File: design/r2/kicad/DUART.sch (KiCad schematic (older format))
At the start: 17 parts, among them IC4 XR68C681CJTR-F, J1 UART_A, J2 UART_B, J4 Conn_01x06, J7 Conn_01x01_Male, Q1 Crystal

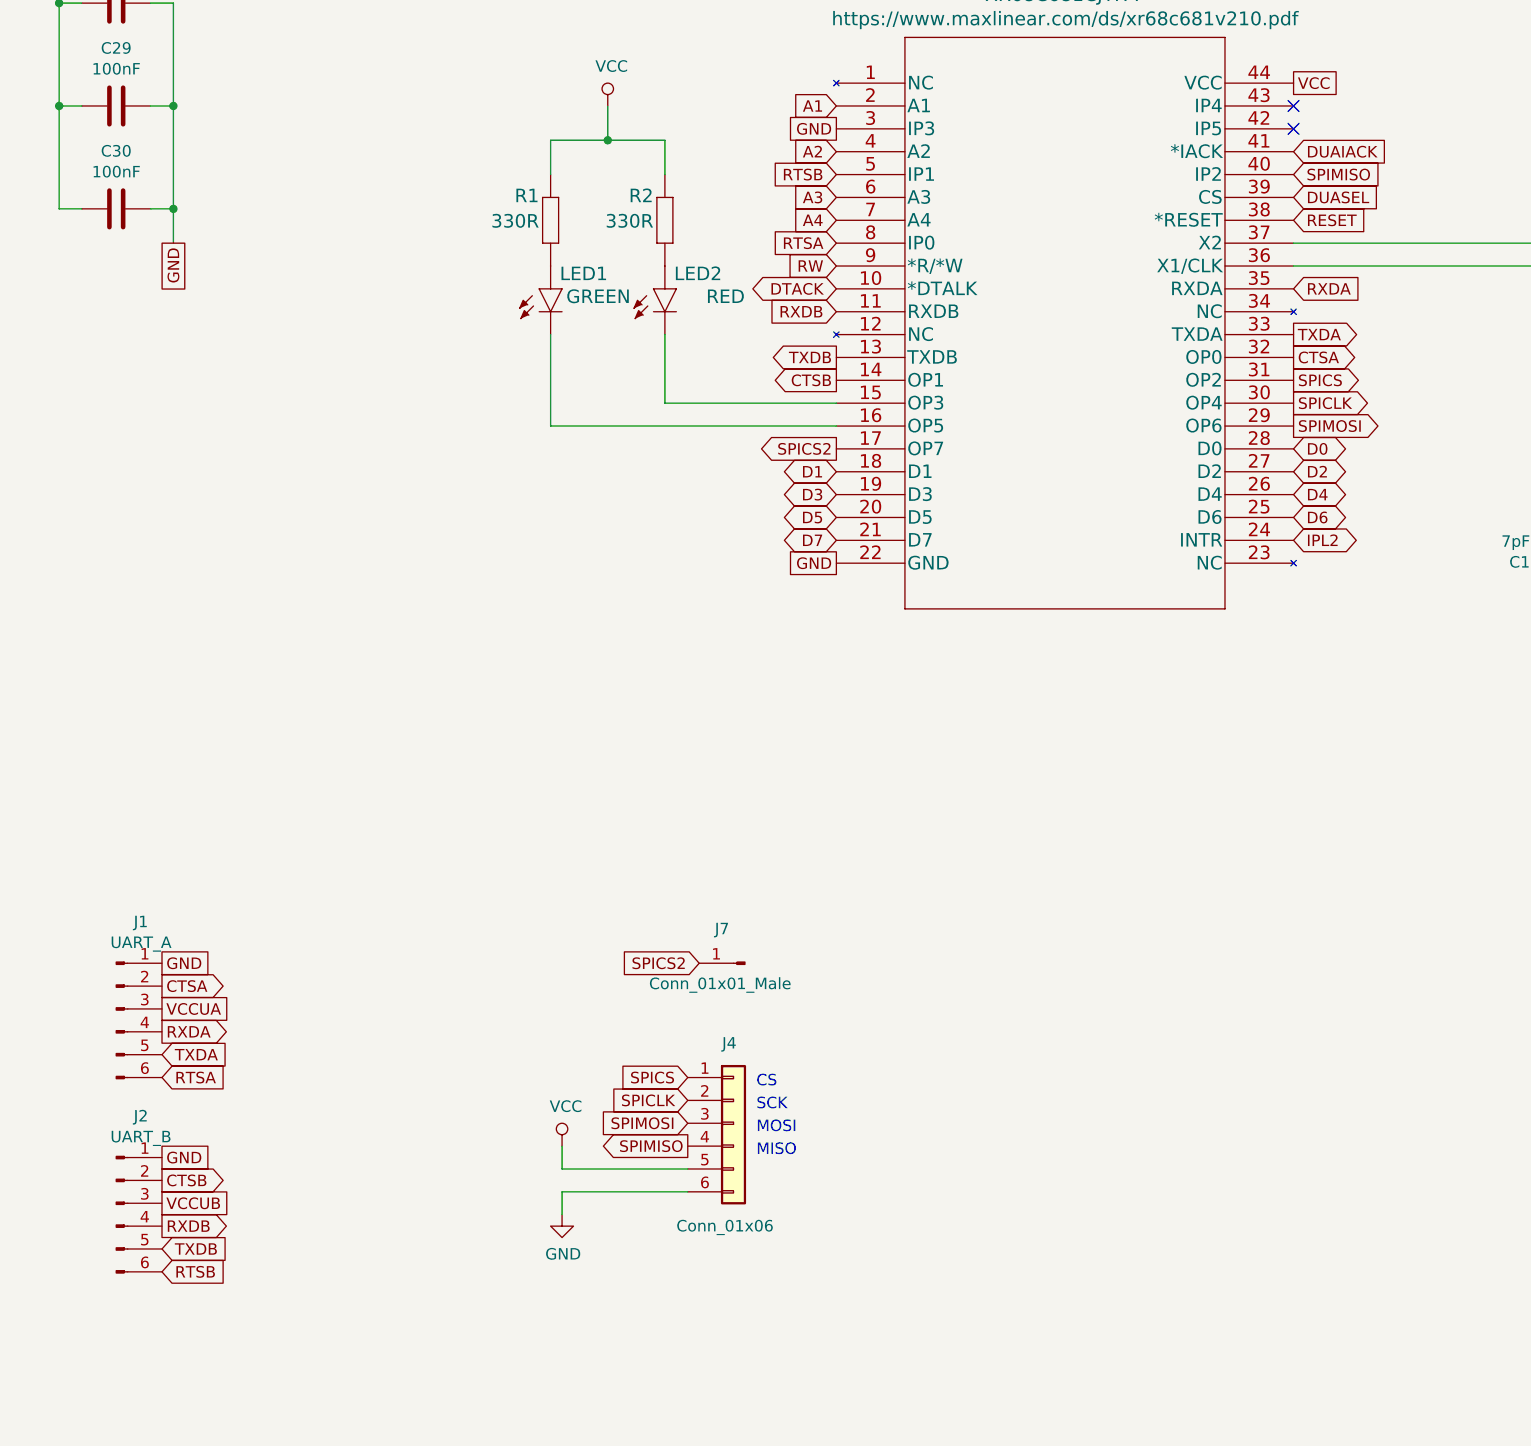
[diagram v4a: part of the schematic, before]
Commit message: Fix CTS/RTS labelling
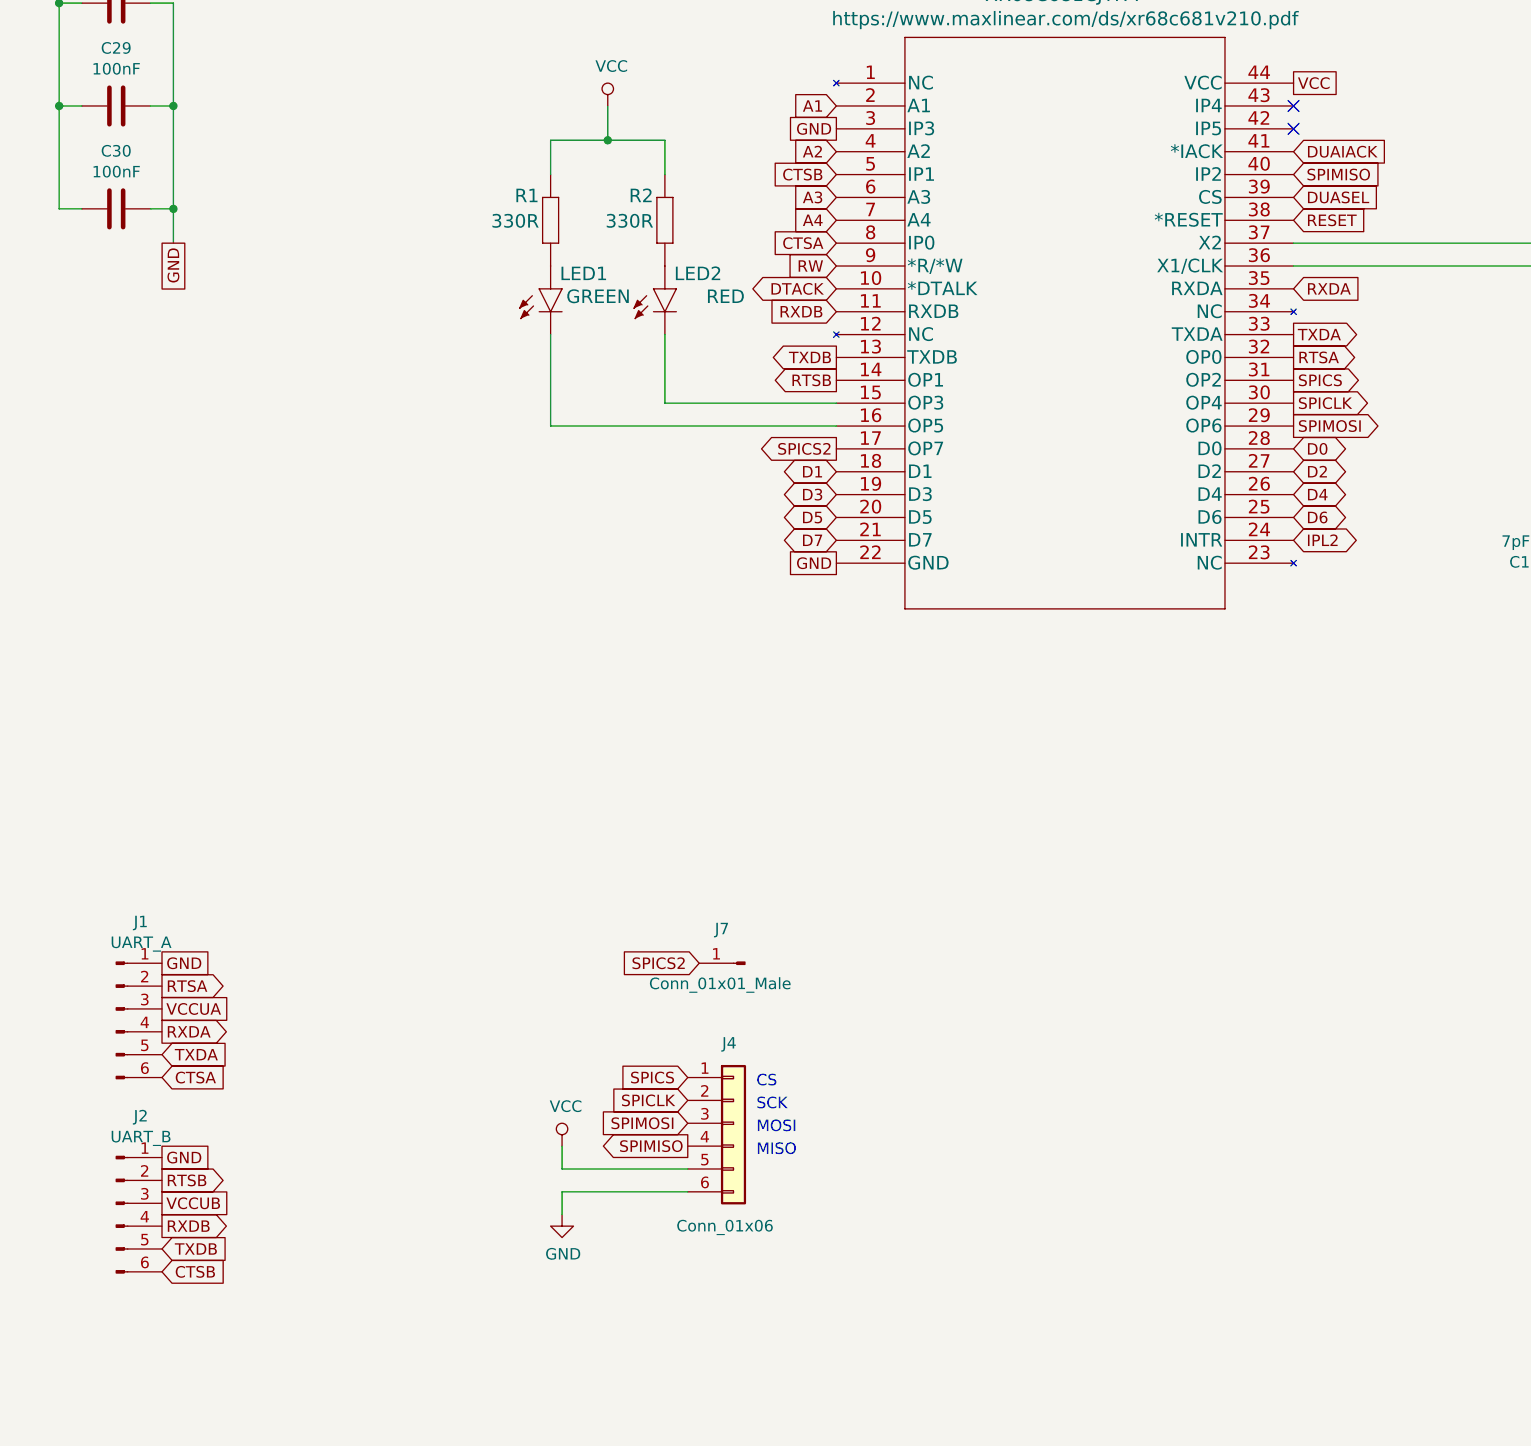
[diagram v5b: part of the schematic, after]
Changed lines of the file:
@@
 GND
 Text GLabel 1450 5750 2    50   Output ~ 0
-CTSA
+RTSA
 Text GLabel 1450 6050 2    50   Input ~ 0
 TXDA
@@
 GND
 Text GLabel 1450 6600 2    50   Output ~ 0
-CTSB
+RTSB
 Text GLabel 1450 6900 2    50   Input ~ 0
 TXDB
@@
 SPIMOSI
 Text GLabel 4400 2500 0    50   Input ~ 0
-RTSA
+CTSA
 Text GLabel 4400 2200 0    50   Input ~ 0
-RTSB
+CTSB
 Text GLabel 6400 2200 2    50   Input ~ 0
 SPIMISO
@@
 GND
 Text GLabel 6400 3000 2    50   Output ~ 0
-CTSA
+RTSA
 Text GLabel 4400 3100 0    50   Output ~ 0
-CTSB
+RTSB
 $Comp
 L Device:C C30
@@
 	9500 5650 9700 5650
 Text GLabel 1450 6150 2    50   Input ~ 0
-RTSA
+CTSA
 Text GLabel 1450 7000 2    50   Input ~ 0
-RTSB
+CTSB
 $Comp
 L rosco_m68k-eagle-import:R-EU_0207_10 R?

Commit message: Bite the bullet and do IPL properly...
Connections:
- net labels added: DUAIRQ
- net labels removed: IPL2
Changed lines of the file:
@@
 Sheet 3 7
 Title "ROSCO_M68K GENERAL PURPOSE MC68010 COMPUTER"
-Date "2021-10-08"
-Rev "2.0"
+Date "2021-10-22"
+Rev "2.1"
 Comp "The Really Old-School Company Limited"
 Comment1 "OSHWA UK000006 (https://certification.oshwa.org/uk000006.html)"
@@
 	8200 2500 6400 2500
 Text GLabel 6400 3800 2    50   3State ~ 0
-IPL2
+DUAIRQ
 NoConn ~ 6400 1900
 NoConn ~ 6400 2000

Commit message: Add value for Q1
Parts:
- Q1: value Crystal -> 3.6864MHz
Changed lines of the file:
@@
 P 7900 3150
 F 0 "Q1" H 7900 3418 50  0000 C CNN
-F 1 "Crystal" H 7900 3327 50  0000 C CNN
+F 1 "3.6864MHz" H 7900 3327 50  0000 C CNN
 F 2 "Crystal:Crystal_HC49-4H_Vertical" H 7900 3150 50  0001 C CNN
 F 3 "~" H 7900 3150 50  0001 C CNN

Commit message: Super-minor tidy-up
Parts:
- C1, C2: footprint rosco_m68k:C2.5-3 -> rosco_m68k:C2.5_or_3.5-3
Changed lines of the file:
@@
 F 0 "C1" H 7665 3896 50  0000 L CNN
 F 1 "7pF" H 7665 3805 50  0000 L CNN
-F 2 "rosco_m68k:C2.5-3" H 7588 3700 50  0001 C CNN
+F 2 "rosco_m68k:C2.5_or_3.5-3" H 7588 3700 50  0001 C CNN
 F 3 "~" H 7550 3850 50  0001 C CNN
 	1    7550 3850
@@
 F 0 "C2" H 8315 3896 50  0000 L CNN
 F 1 "7pF" H 8315 3805 50  0000 L CNN
-F 2 "rosco_m68k:C2.5-3" H 8238 3700 50  0001 C CNN
+F 2 "rosco_m68k:C2.5_or_3.5-3" H 8238 3700 50  0001 C CNN
 F 3 "~" H 8200 3850 50  0001 C CNN
 	1    8200 3850
-	1    0    0    -1
+	-1   0    0    1
 $EndComp
 Wire Wire Line
